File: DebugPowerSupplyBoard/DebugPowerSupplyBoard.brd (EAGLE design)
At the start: 160 x 100 mm, 277 parts, among them IC1 LD117AV33, IC2 7805T

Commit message: Progress was made
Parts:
- added J1: (no value), CustomEuroCard:VG96KB
- moved IC1 852.5 mm to (952.5, 261.6)
- moved IC2 852.5 mm to (946.1, 243.4)
- moved C3 852.3 mm to (966.2, 240.8)
- moved C4 852.3 mm to (976.4, 240.8)
- moved C1 846.9 mm to (960.1, 261.6)
- moved C2 841.6 mm to (963.9, 261.6)
- moved U$249 284.5 mm to (-157.5, 15.2), flipped to the bottom
- moved U$246 279.4 mm to (-154.9, 17.8), flipped to the bottom
- moved U$247 279.4 mm to (-154.9, 20.3), flipped to the bottom
- moved U$248 279.4 mm to (-154.9, 15.2), flipped to the bottom
- moved U$250 279.4 mm to (-154.9, 12.7), flipped to the bottom
- moved U$255 279.4 mm to (-154.9, 10.2), flipped to the bottom
- moved U$244 274.3 mm to (-152.4, 20.3), flipped to the bottom
- moved U$245 274.3 mm to (-152.4, 17.8), flipped to the bottom
- moved U$251 274.3 mm to (-152.4, 12.7), flipped to the bottom
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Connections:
- new net A1: J1.A1, J2.A1
- new net A10: J1.A10, J2.A10
- new net A2: J1.A2, J2.A2
- new net B10: J1.B10, J2.B10
- new net C10: J1.C10, J2.C10
- new net N$10: J1.A17, J2.A17
- new net N$100: J1.A31, J2.A31
- new net N$101: J1.B31, J2.B31
- new net N$102: J1.C31, J2.C31
- new net N$103: J1.A32, J2.A32
- new net N$104: J1.B32, J2.B32
- new net N$105: J1.C32, J2.C32
- new net N$11: J1.B17, J2.B17
- new net N$12: J1.C17, J2.C17
- new net N$13: J1.A18, J2.A18
- new net N$14: J1.B18, J2.B18
- new net N$16: J1.C18, J2.C18
- new net N$18: J1.A19, J2.A19
- new net N$19: J1.B19, J2.B19
- new net N$20: J1.C19, J2.C19
- new net N$21: J1.A20, J2.A20
- new net N$22: J1.B20, J2.B20
- new net N$23: J1.C20, J2.C20
- new net N$25: J1.A21, J2.A21
- new net N$39: J1.B21, J2.B21
- new net N$4: J1.A15, J2.A15
- new net N$40: J1.C21, J2.C21
- new net N$44: J1.A22, J2.A22
- new net N$45: J1.B22, J2.B22
- new net N$47: J1.C22, J2.C22
- new net N$49: J1.A23, J2.A23
- new net N$5: J1.B15, J2.B15
- new net N$50: J1.B23, J2.B23
- new net N$51: J1.C23, J2.C23
- new net N$52: J1.A24, J2.A24
- new net N$53: J1.B24, J2.B24
- new net N$54: J1.C24, J2.C24
- new net N$55: J1.A25, J2.A25
- new net N$56: J1.B25, J2.B25
- new net N$57: J1.C25, J2.C25
- new net N$58: J1.A26, J2.A26
- new net N$6: J1.C15, J2.C15
- new net N$67: J1.B26, J2.B26
- new net N$69: J1.C26, J2.C26
- new net N$7: J1.A16, J2.A16
- new net N$70: J1.A27, J2.A27
- new net N$79: J1.B27, J2.B27
- new net N$8: J1.B16, J2.B16
- new net N$86: J1.C27, J2.C27
- new net N$87: J1.A28, J2.A28
- new net N$89: J1.B28, J2.B28
- new net N$9: J1.C16, J2.C16
- new net N$90: J1.C28, J2.C28
- new net N$92: J1.A29, J2.A29
- new net N$94: J1.B29, J2.B29
- new net N$95: J1.C29, J2.C29
- new net N$97: J1.A30, J2.A30
- new net N$98: J1.B30, J2.B30
- new net N$99: J1.C30, J2.C30
- net +3V3: now also J1.B1, J1.C1
- net +5V: now also J1.C4
- net +5V_DIFF: now also J1.A8
- net +7V_DIFF: now also J1.A9
- net -5V_DIFF: now also J1.C8
- net -7V_DIFF: now also J1.C9
- net CHARGE_PROBE_0: now also J1.A14
- net CHARGE_PROBE_1: now also J1.B14
- net CONDUCTIVITY_ENABLE: now also J1.C14
- net GND: now also J1.A5, J1.A6, J1.A7, J1.B11, J1.B12, J1.B13
- net GND_3V3: now also J1.B2, J1.C2
- net GND_5V: now also J1.C3
- net GND_5V_DIFF: now also J1.B8
- net GND_7V_DIFF: now also J1.B9
- net GND_TEMP: now also J1.B3
- net I_1_H: now also J1.C5
- net I_1_L: now also J1.B5
- net I_2_H: now also J1.C6
- net I_2_L: now also J1.B6
- net I_3_H: now also J1.C7
- net I_3_L: now also J1.B7
- net PROBE_DIFF_HOR: now also J1.A13
- net PROBE_DIFF_VERT: now also J1.C13
- net PROBE_HOR_1_RIGHT: now also J1.A11
- net PROBE_HOR_2_LEFT: now also J1.A12
- net PROBE_VERT_1_UP: now also J1.C11
- net PROBE_VERT_2_DOWN: now also J1.C12
- net TEMP_1: now also J1.B4
- net TEMP_2: now also J1.A4
- net TEMP_3: now also J1.A3
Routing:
- net GND_3V3: track 28.8 -> 313.9 mm
- net +3V3: track 31.3 -> 309.2 mm
- net TEMP_3: track 0.00 -> 165.7 mm
- net A2: track 0.00 -> 164.7 mm
- net GND_TEMP: track 0.00 -> 159.6 mm
- net A1: track 0.00 -> 159.6 mm
- net GND_5V: track 68.2 -> 213.3 mm
- net TEMP_2: track 0.00 -> 19.4 mm
- net I_1_L: track 0.00 -> 16.8 mm
- net +5V: track 40.7 -> 49.9 mm
- net VIN: track 20.7 -> 14.8 mm

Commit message: Changed the capacitors used to be ones which are readily avaliable from DigiKey
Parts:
- added C5, C6: 3.3uF, rcl:C050-055X075
- C2: value 10uF -> 3.3uF; device rcl:C050-025X075 -> rcl:C050-055X075
- C3: device rcl:C050-025X075 -> rcl:C050-035X075
- moved C4 21.6 mm to (998.0, 240.8)
- moved C2 5.08 mm to (969.0, 261.6)
- moved C1 2.54 mm to (962.7, 261.6)
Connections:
- net +3V3: now also C5.1, C6.1
- net GND_3V3: now also C5.2, C6.2
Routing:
- net N$97: track 0.00 -> 165.7 mm
- net +5V: track 49.9 -> 209.7 mm
- net N$103: track 0.00 -> 159.6 mm
- net TEMP_1: track 0.00 -> 155.6 mm
- net N$101: track 0.00 -> 154.5 mm
- net N$99: track 0.00 -> 149.4 mm
- net TEMP_2: track 19.4 -> 163.2 mm
- net N$105: track 0.00 -> 143.3 mm
- net GND_5V: track 213.3 -> 256.5 mm
- net GND_3V3: track 313.9 -> 340.5 mm
- net +3V3: track 309.2 -> 335.9 mm
- net VIN: track 14.8 -> 17.3 mm

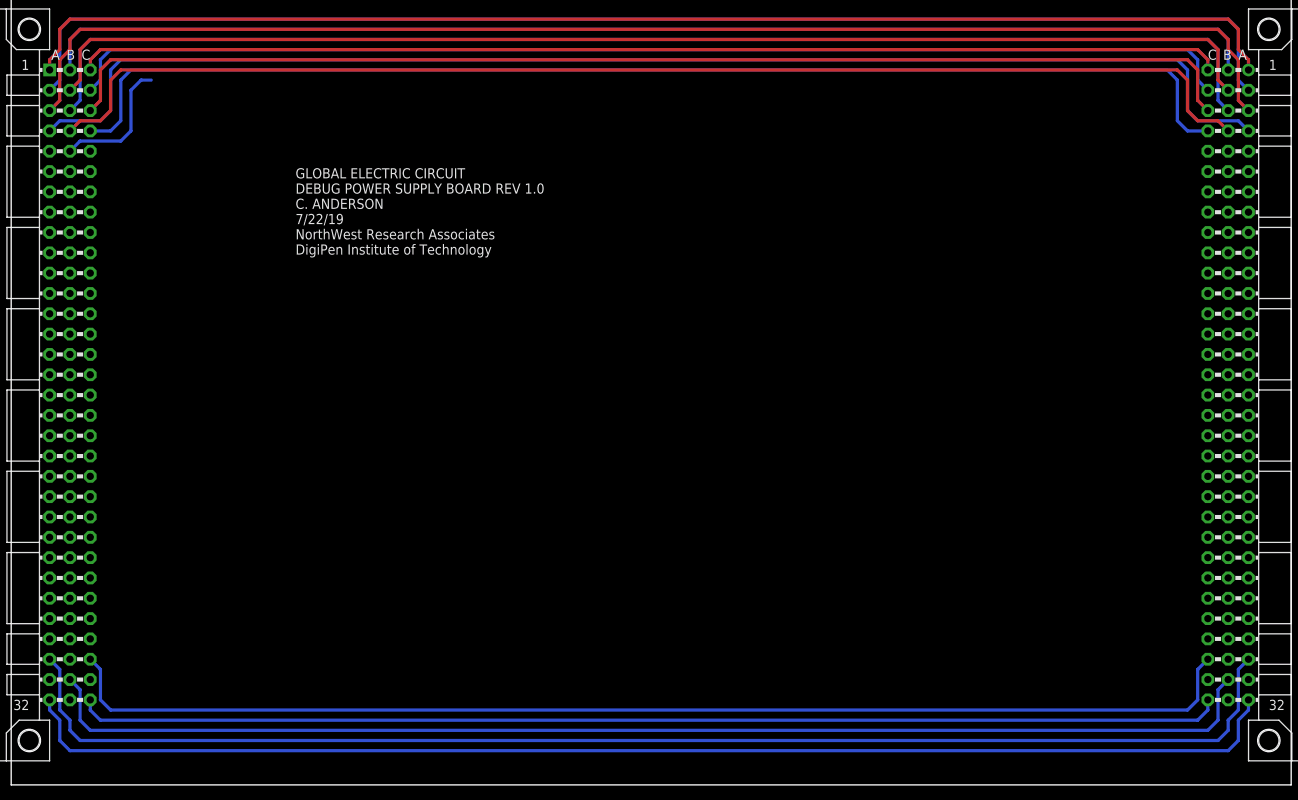
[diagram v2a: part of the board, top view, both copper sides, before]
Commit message: Routed the upper half of the traces for the board
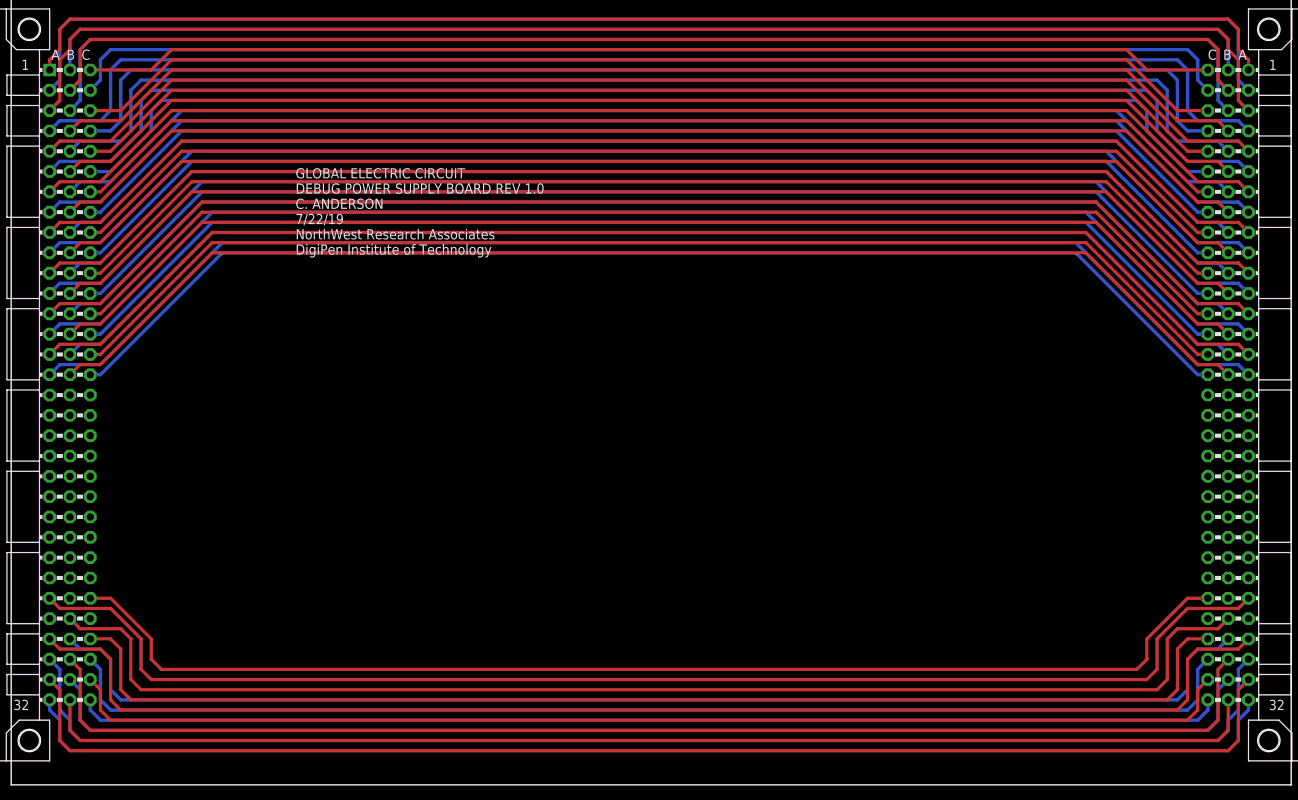
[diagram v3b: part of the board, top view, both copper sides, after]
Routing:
- net GND: track 0.00 -> 945.2 mm
- net N$100: track 0.00 -> 164.7 mm
- net N$7: track 0.00 -> 163.5 mm
- net N$92: track 0.00 -> 163.2 mm
- net N$70: track 0.00 -> 162.7 mm
- net N$4: track 0.00 -> 162.5 mm
- net CHARGE_PROBE_0: track 0.00 -> 162.5 mm
- net PROBE_HOR_2_LEFT: track 0.00 -> 161.4 mm
- net PROBE_DIFF_HOR: track 0.00 -> 161.4 mm
- net PROBE_HOR_1_RIGHT: track 0.00 -> 160.4 mm
- net A10: track 0.00 -> 160.4 mm
- net N$98: track 0.00 -> 159.6 mm
- net +7V_DIFF: track 0.00 -> 159.3 mm
- net +5V_DIFF: track 0.00 -> 159.3 mm
- net N$89: track 0.00 -> 158.1 mm
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
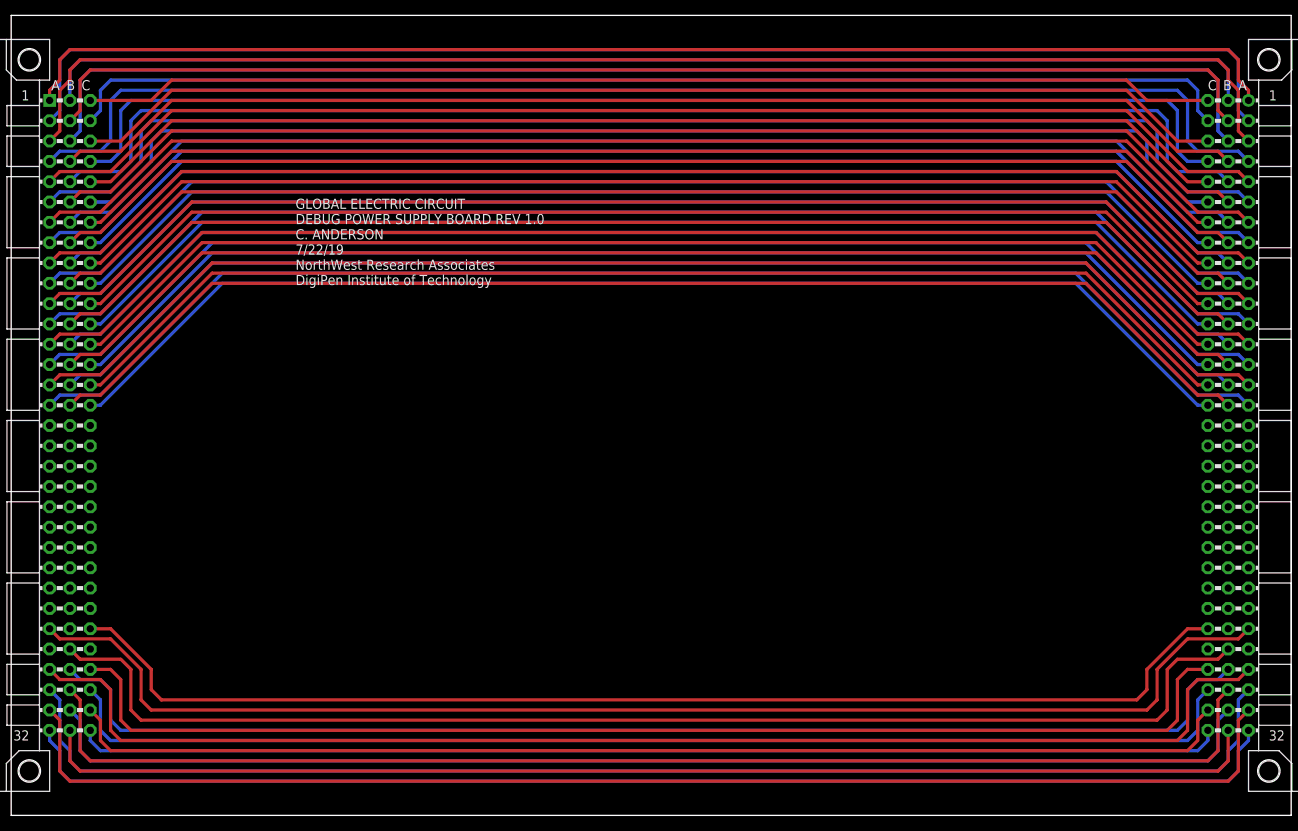
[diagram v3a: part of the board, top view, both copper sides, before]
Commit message: Moved all the traces near the bottom of the board
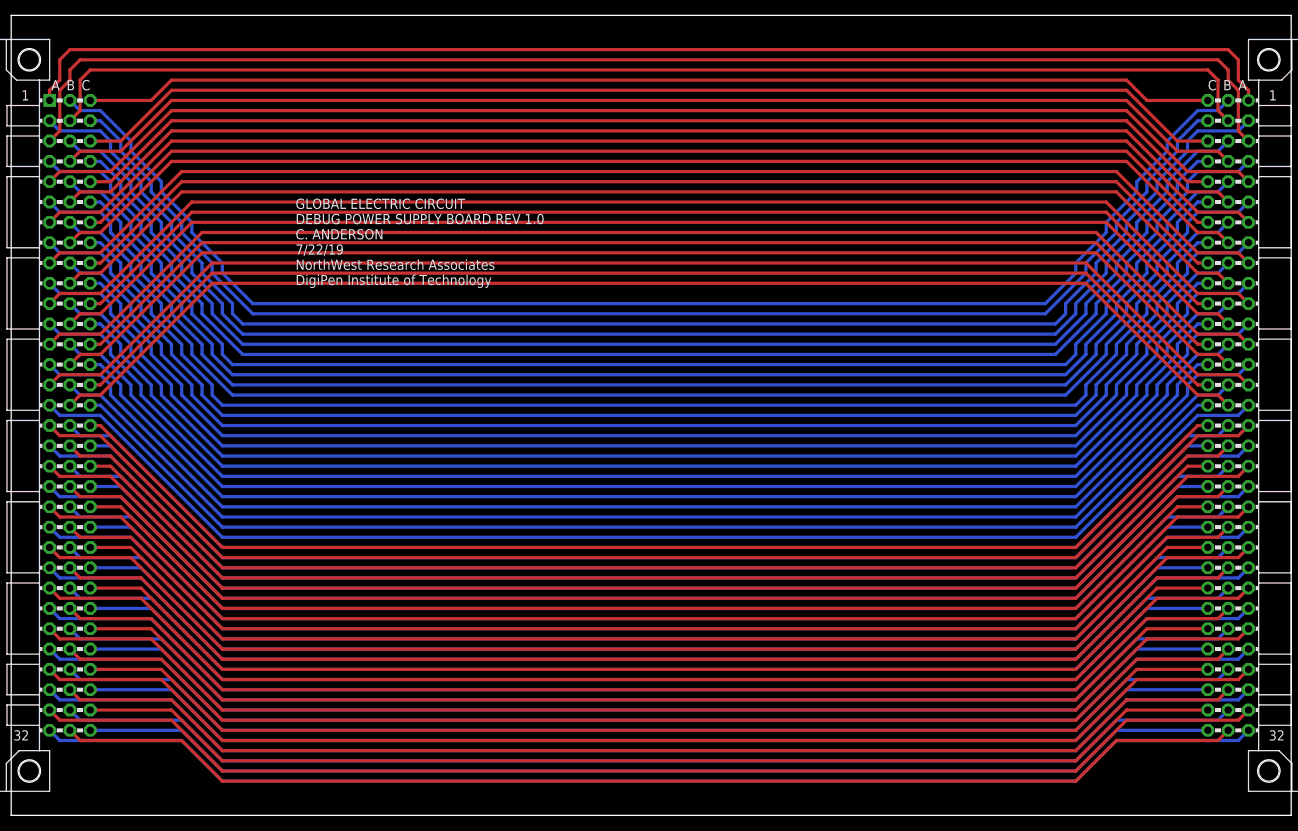
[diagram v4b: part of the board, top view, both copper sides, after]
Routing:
- net N$10: track 0.00 -> 163.5 mm
- net N$18: track 0.00 -> 162.5 mm
- net N$13: track 0.00 -> 162.5 mm
- net N$25: track 0.00 -> 161.4 mm
- net N$21: track 0.00 -> 161.4 mm
- net N$49: track 0.00 -> 160.4 mm
- net N$44: track 0.00 -> 160.4 mm
- net N$55: track 0.00 -> 159.3 mm
- net N$52: track 0.00 -> 159.3 mm
- net N$58: track 0.00 -> 158.3 mm
- net N$14: track 0.00 -> 157.4 mm
- net N$11: track 0.00 -> 157.4 mm
- net N$87: track 0.00 -> 157.2 mm
- net N$22: track 0.00 -> 156.4 mm
- net N$19: track 0.00 -> 156.4 mm
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
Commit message: Added the XT60 connector. Almost done with this cursed board
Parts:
- added U$6: XT60, XT60:XT60
- moved C4 942.0 mm to (71.1, 72.4)
- moved C6 936.8 mm to (67.3, 82.5)
- moved IC1 935.8 mm to (34.3, 81.3), turned to 180 degrees
- moved C5 935.5 mm to (59.7, 82.5)
- moved C1 935.5 mm to (44.5, 82.5)
- moved C2 934.3 mm to (52.1, 82.5)
- moved C3 916.3 mm to (66.0, 69.8)
- moved IC2 911.5 mm to (50.8, 72.4)
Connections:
- net N$10 renamed A17
- net N$100 renamed A31
- net N$101 renamed B31
- net N$102 renamed C31
- net N$103 renamed A32
- net N$104 renamed B32
- net N$105 renamed C32
- net N$11 renamed B17
- net N$12 renamed C17
- net N$13 renamed A18
- net N$14 renamed B18
- net N$16 renamed C18
- net N$18 renamed A19
- net N$19 renamed B19
- net N$20 renamed C19
- net N$21 renamed A20
- net N$22 renamed B20
- net N$23 renamed C20
- net N$25 renamed A21
- net N$39 renamed B21
- net N$4 renamed A15
- net N$40 renamed C21
- net N$44 renamed A22
- net N$45 renamed B22
- net N$47 renamed C22
- net N$49 renamed A23
- net N$5 renamed B15
- net N$50 renamed B23
- net N$51 renamed C23
- net N$52 renamed A24
- net N$53 renamed B24
- net N$54 renamed C24
- net N$55 renamed A25
- net N$56 renamed B25
- net N$57 renamed C25
- net N$58 renamed A26
- net N$6 renamed C15
- net N$67 renamed B26
- net N$69 renamed C26
- net N$7 renamed A16
- net N$70 renamed A27
- net N$79 renamed B27
- net N$8 renamed B16
- net N$86 renamed C27
- net N$87 renamed A28
- net N$89 renamed B28
- net N$9 renamed C16
- net N$90 renamed C28
- net N$92 renamed A29
- net N$94 renamed B29
- net N$95 renamed C29
- net N$97 renamed A30
- net N$98 renamed B30
- net N$99 renamed C30
- net GND: now also U$6.-
- net VIN: now also U$6.+
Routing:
- net GND: track 970.1 -> 1350.9 mm, vias 0 -> 21
- net GND_3V3: track 359.3 -> 559.2 mm, vias 0 -> 7
- net +3V3: track 352.7 -> 512.3 mm, vias 0 -> 4
- net VIN: track 17.3 -> 84.6 mm
- net +5V: track 222.3 -> 272.5 mm, vias 0 -> 4
- net TEMP_1: track 151.1 -> 175.1 mm
- net I_2_L: track 152.1 -> 175.1 mm
- net I_1_H: track 146.0 -> 169.0 mm
- net I_3_H: track 147.1 -> 169.0 mm
- net A1: track 159.6 -> 180.9 mm
- net GND_5V_DIFF: track 153.2 -> 174.4 mm
- net -7V_DIFF: track 148.1 -> 169.0 mm
- net +7V_DIFF: track 159.3 -> 180.2 mm
- net B10: track 154.2 -> 174.4 mm
- net PROBE_VERT_1_UP: track 149.2 -> 168.2 mm
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
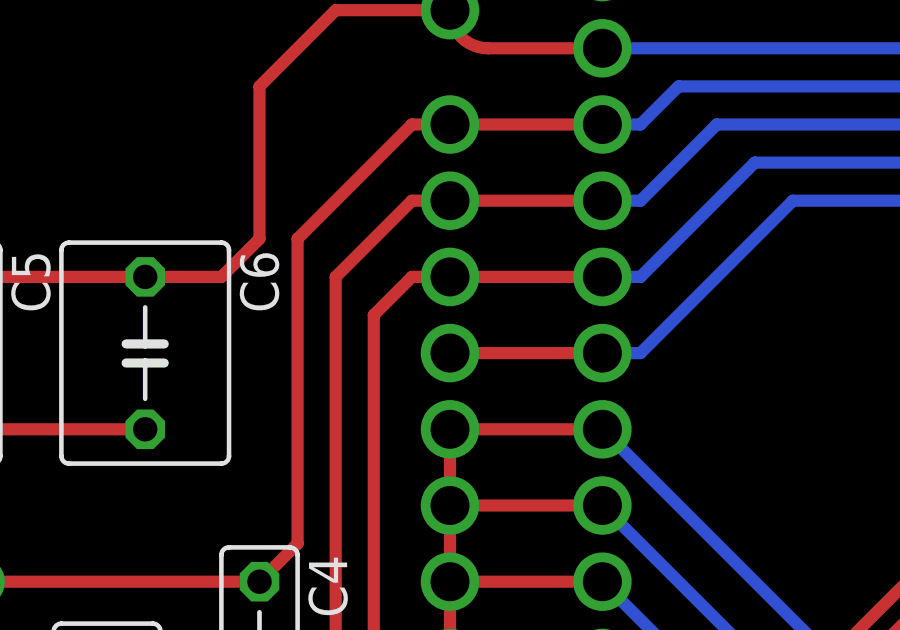
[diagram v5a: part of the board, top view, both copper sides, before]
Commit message: All the grounds are 'connected'. Just about to rename them to finalize it
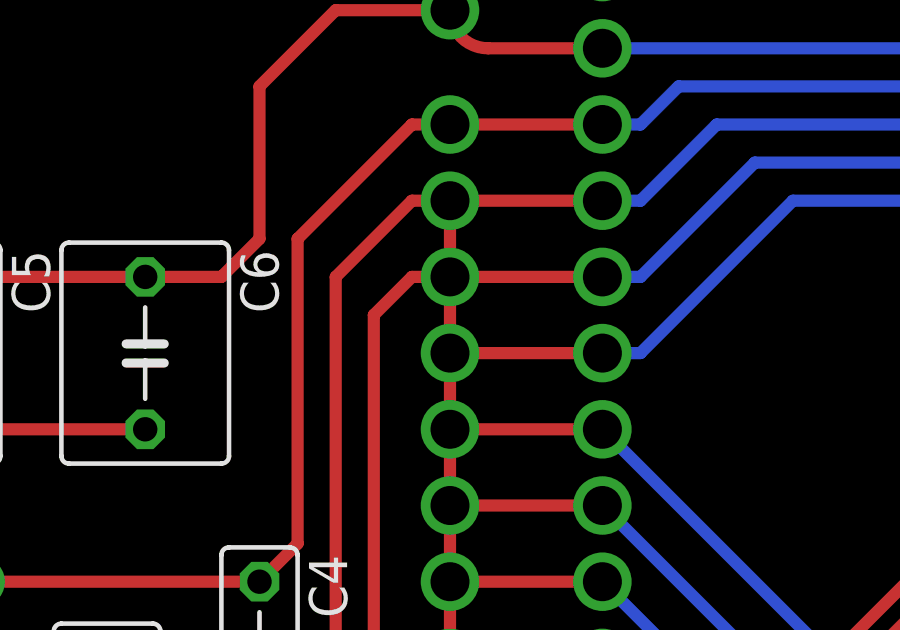
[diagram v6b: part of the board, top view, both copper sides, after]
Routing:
- net GND_3V3: track 559.2 -> 564.3 mm
- net GND: track 1350.9 -> 1353.4 mm
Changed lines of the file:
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@@
 <contactref element="U$6" pad="-"/>
 <wire x1="7.62" y1="58.42" x2="16.186" y2="91.44" width="0" layer="19" extent="1-1"/>
+<wire x1="77.47" y1="80.01" x2="77.47" y2="82.55" width="0.4064" layer="1"/>
 </signal>
 <signal name="CONDUCTIVITY_ENABLE">
@@
 <wire x1="40.64" y1="80.01" x2="41.91" y2="81.28" width="0.4064" layer="1"/>
 <wire x1="11.43" y1="85.09" x2="11.43" y2="86.36" width="0" layer="19" extent="1-16"/>
+<wire x1="77.47" y1="85.09" x2="77.47" y2="87.63" width="0.4064" layer="1"/>
+<wire x1="77.47" y1="82.55" x2="77.47" y2="85.09" width="0.4064" layer="1"/>
 </signal>
 <signal name="A1">
